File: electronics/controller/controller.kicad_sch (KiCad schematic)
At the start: 55 parts, among them J1 AZ_STEPPER_TEMP, J10 USB C, J11 PWR IN, J2 EL_STEPPER_TEMP, J3 TEMP_PROBE, J4 I2C, J5 AZ_ENDSTOP, J6 UART, J7 EL_ENDSTOP1, J8 EL_SERVO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

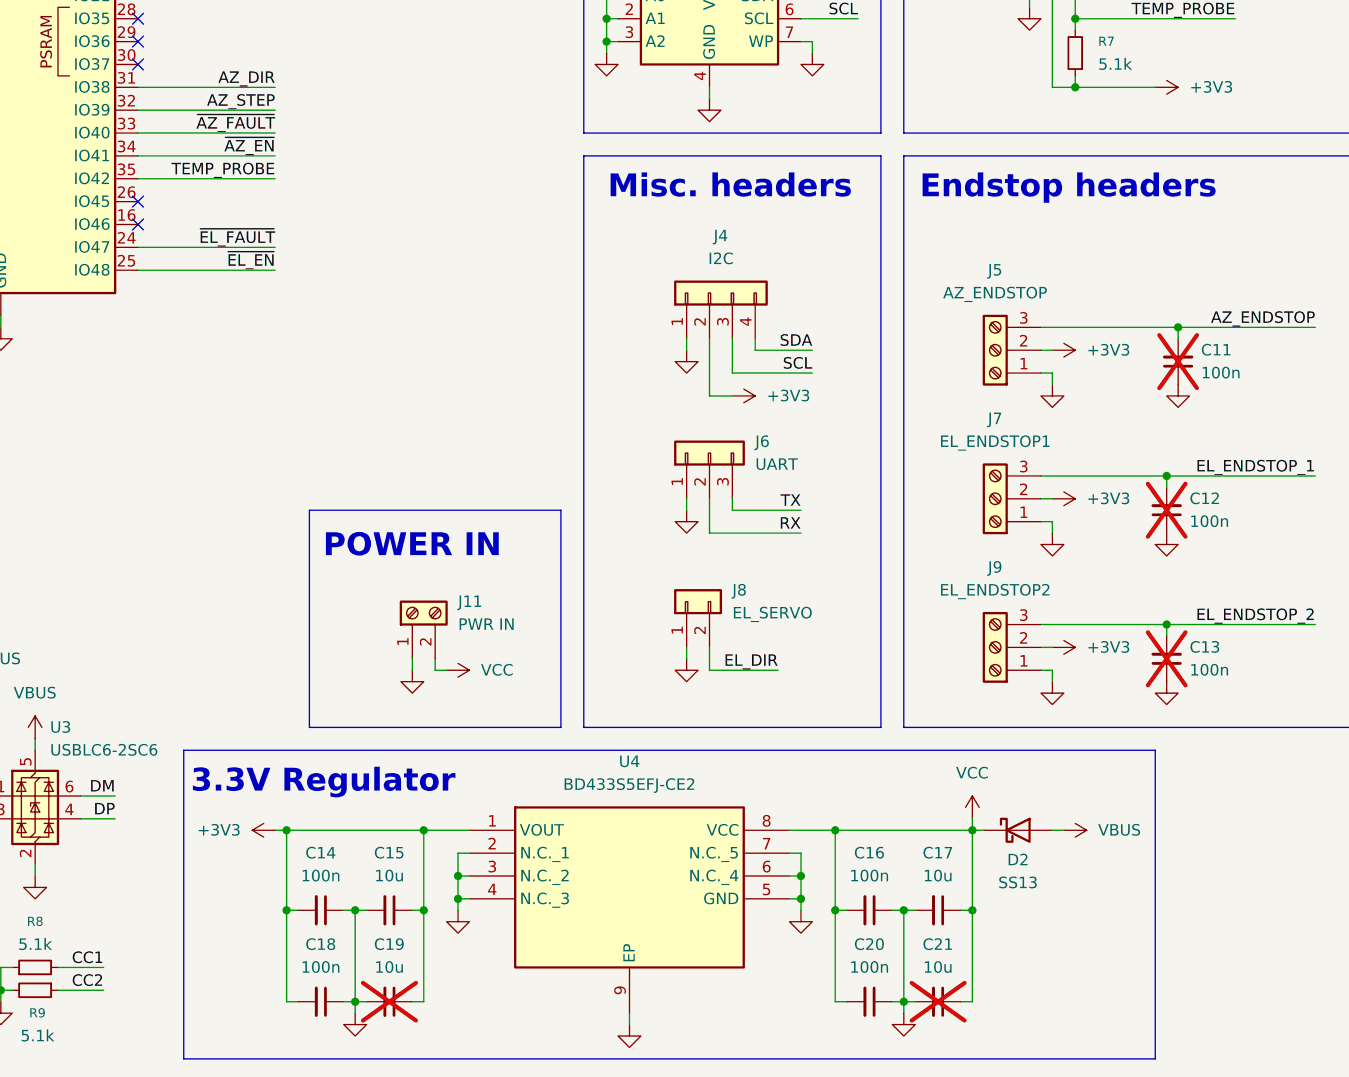
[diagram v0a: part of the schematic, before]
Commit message: Switch to Buck converter
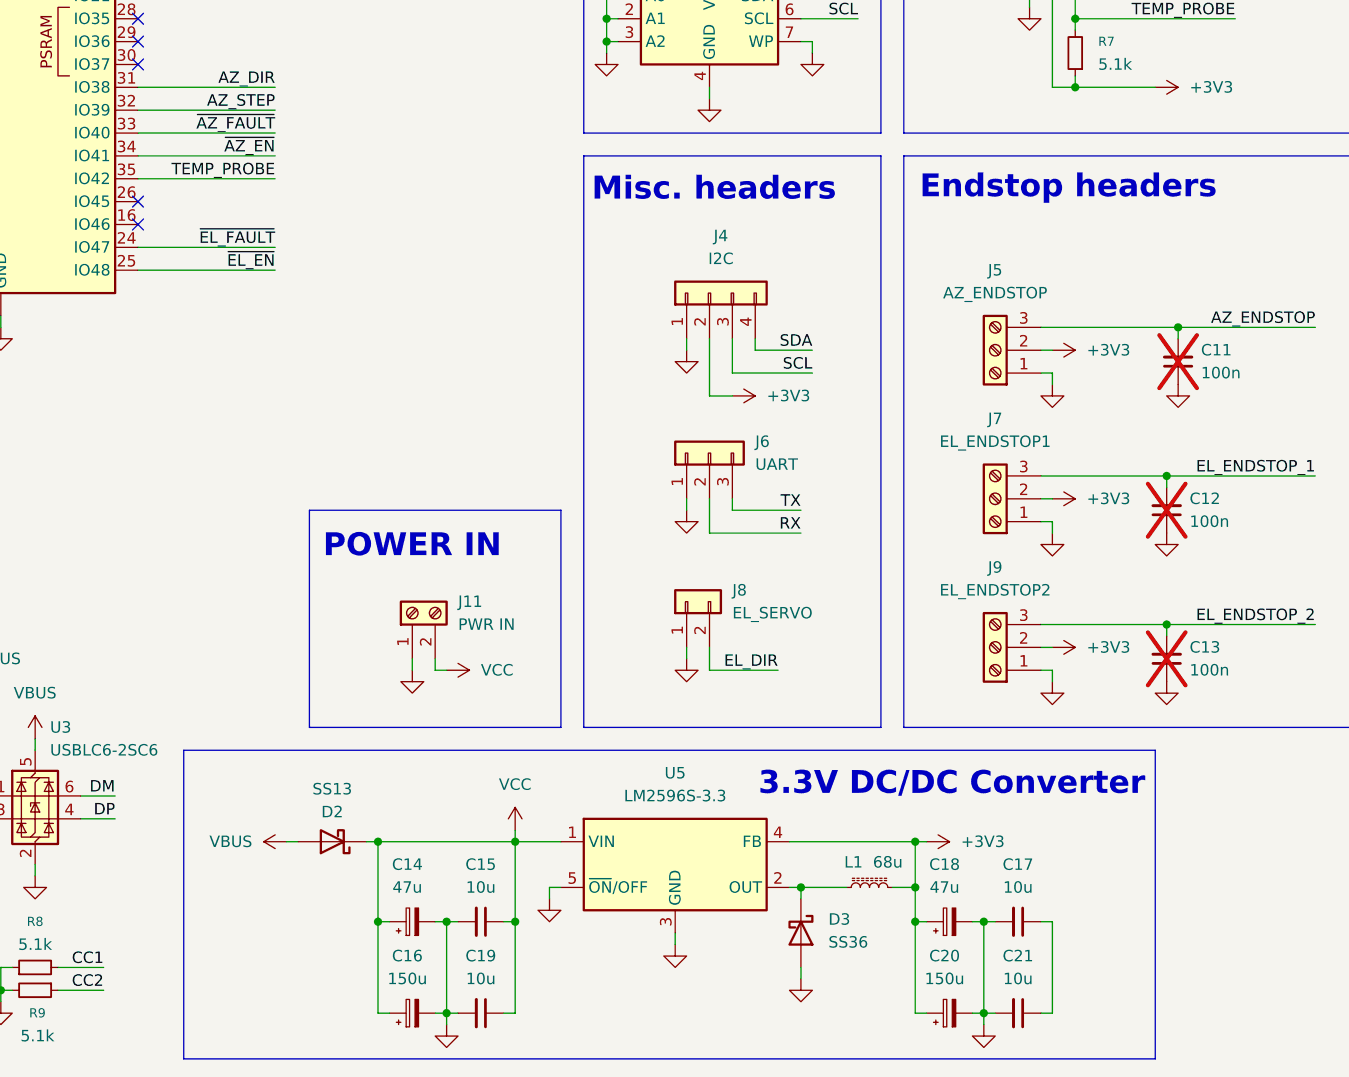
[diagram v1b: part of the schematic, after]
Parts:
- removed C14, C16, C18, C20: 100n, Capacitor_SMD:C_0402_1005Metric, symbol Device:C_Small
- removed U4: BD433S5EFJ-CE2, SOIC127P600X100-9N, symbol SamacSys_Parts:BD433S5EFJ-CE2
- added C14, C18: 47u, Capacitor_SMD:CP_Elec_8x10, symbol Device:C_Polarized_Small
- added C16, C20: 150u, Capacitor_SMD:CP_Elec_10x10, symbol Device:C_Polarized_Small
- added D3: SS36, Diode_SMD:D_SMA, symbol Diode:SS36
- added L1: 68u, Inductor_SMD:L_Coilcraft_MSS1260-XXX, symbol Device:L_Ferrite_Small
- added U5: LM2596S-3.3, Package_TO_SOT_SMD:TO-263-5_TabPin3, symbol Regulator_Switching:LM2596S-3.3
- C15, C17: footprint Capacitor_SMD:C_0805_2012Metric -> Capacitor_SMD:C_1210_3225Metric
- C19, C21: footprint Capacitor_SMD:C_0805_2012Metric -> Capacitor_SMD:C_1210_3225Metric; now fitted
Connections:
- net +3V3: now also C18.1, C20.1, L1.2, U5.4 (FB); no longer C15.1, C19.1
- net GND: now also C14.2, C16.2, C18.2, C20.2, D3.2 (A), U5.3 (GND), U5.5 (~{ON}/OFF)
- net VCC: now also C15.1, C19.1, C14.1, C16.1, U5.1 (VIN); no longer C17.1, C21.1
- new net: D3.1 (K), L1.1, U5.2 (OUT)
- new net: C17.1, C21.1
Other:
- note added: "3.3V DC/DC Converter"
- note removed: "3.3V Regulator"
- moved on the sheet: C15, C17, D2

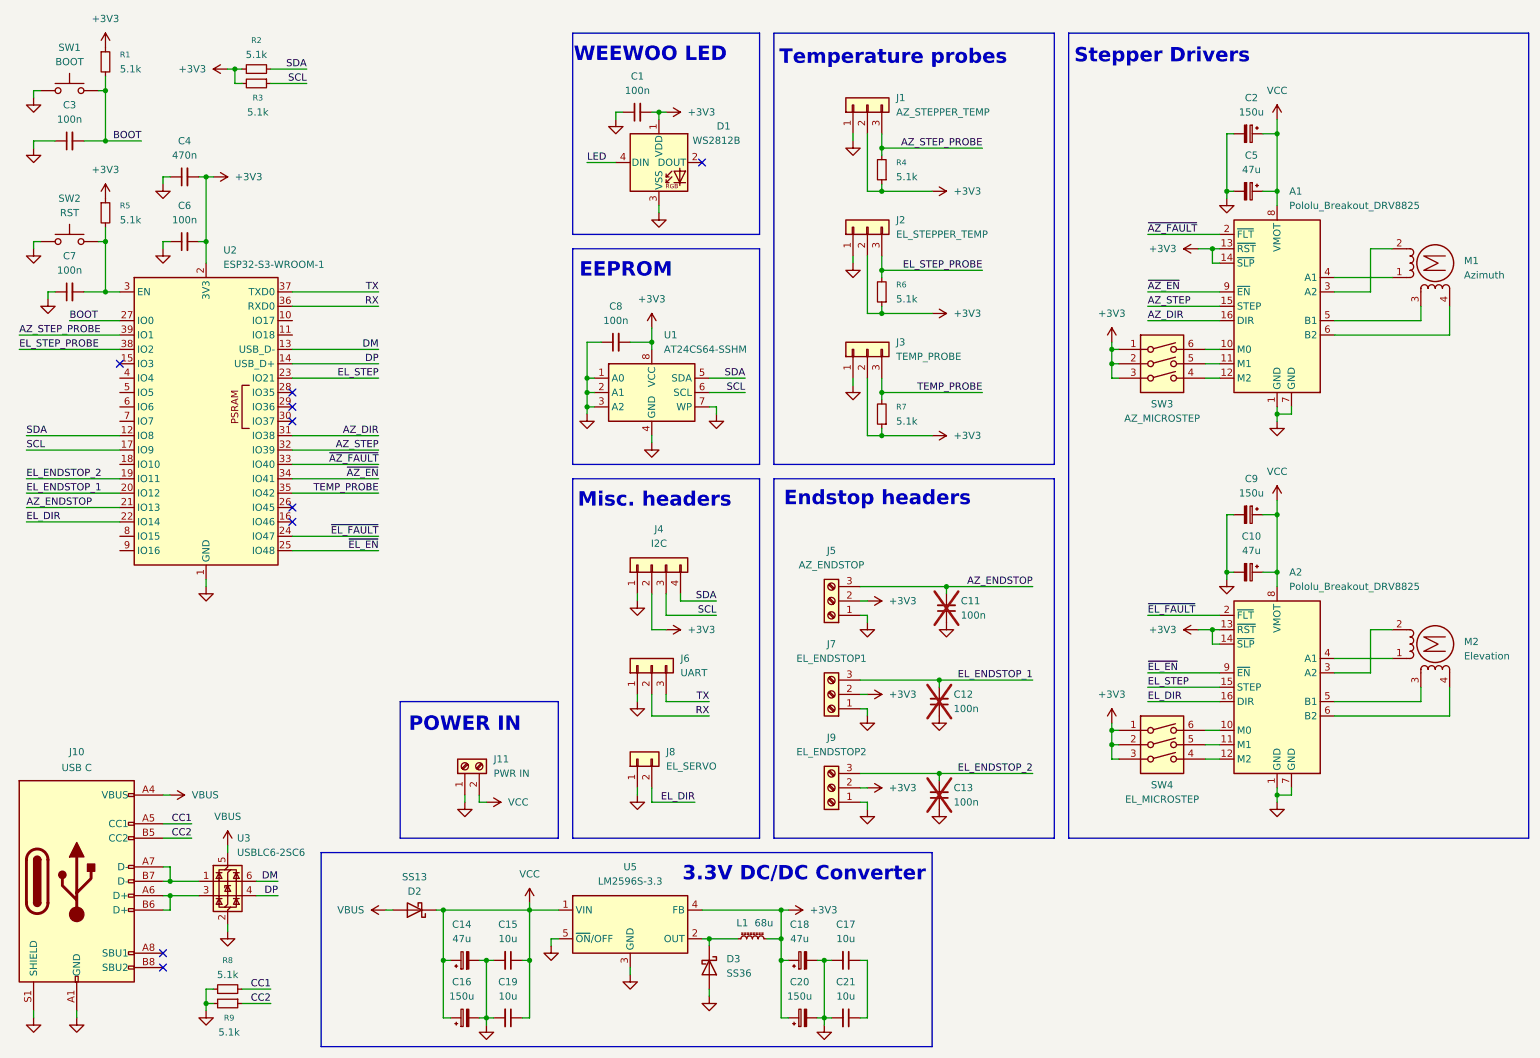
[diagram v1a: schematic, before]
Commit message: Add mounting holes to the schematic
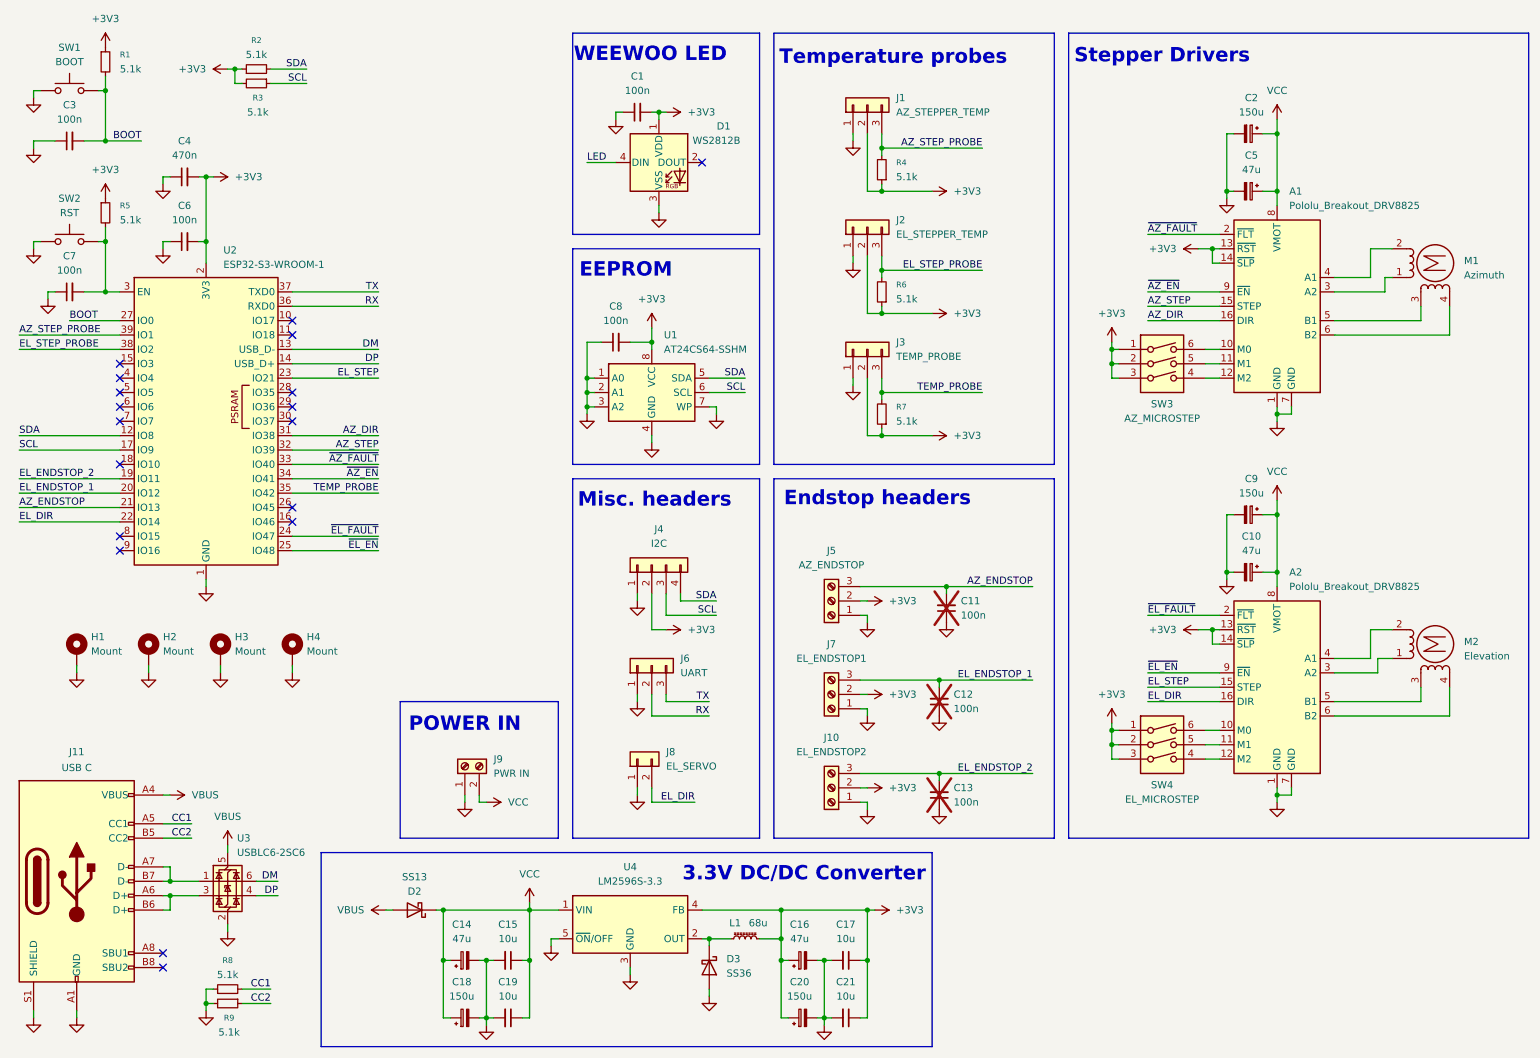
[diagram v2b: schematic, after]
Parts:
- added H1, H2, H3, H4: Mount, MountingHole:MountingHole_2.7mm_M2.5_DIN965_Pad, symbol Mechanical:MountingHole_Pad
- renumbered C18 to C16, C16 to C18, J9 to J10, J10 to J11, J11 to J9, U5 to U4
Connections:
- net +3V3: now also C17.1, C21.1
- net GND: now also H1.1, H2.1, H3.1, H4.1
- net at M2.1: now also A2.3 (A2); no longer A2.4 (A1)
- net at M2.2 (-): now also A2.4 (A1); no longer A2.3 (A2)
- net at M1.1: now also A1.3 (A2); no longer A1.4 (A1)
- net at M1.2 (-): now also A1.4 (A1); no longer A1.3 (A2)
- no-connect marks 9 -> 18
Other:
- moved on the sheet: L1

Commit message: lol
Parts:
- added D4: SMBJ33CA, Diode_SMD:D_SMB, symbol Device:D_TVS_Small
- added JP1: AZ_ADDR_1, Jumper:SolderJumper-3_P1.3mm_Bridged12_RoundedPad1.0x1.5mm_NumberLabels, symbol Jumper:SolderJumper_3_Bridged12
- added JP2: AZ_ADDR_2, Jumper:SolderJumper-3_P1.3mm_Bridged12_RoundedPad1.0x1.5mm_NumberLabels, symbol Jumper:SolderJumper_3_Bridged12
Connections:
- net GND: now also D4.1 (A1)
- net VCC: now also D4.2 (A2)
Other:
- moved on the sheet: C14, C15, C18, C19, D2, J11, R8, R9, U3
